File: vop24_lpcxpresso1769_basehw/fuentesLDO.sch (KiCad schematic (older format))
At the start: 21 parts, among them J101 Conn_01x03_Male, U101 MCP1700T-3302E_TT, U102 MCP1700T-3302E_TT, U103 TPS63001

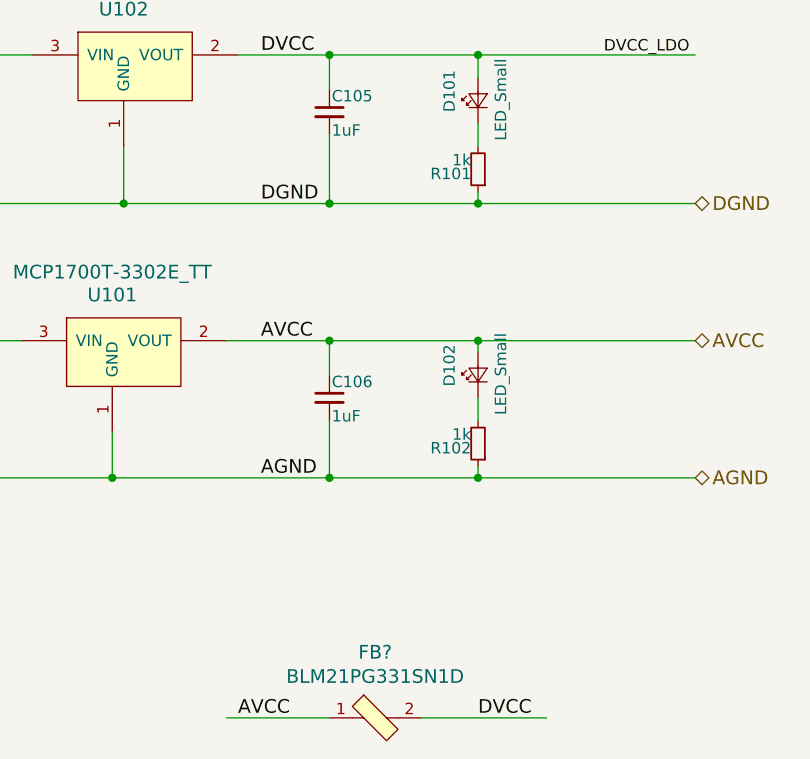
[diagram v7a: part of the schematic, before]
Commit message: Finalizada asociación de todos los footprints. Ver librerías froux-kicad
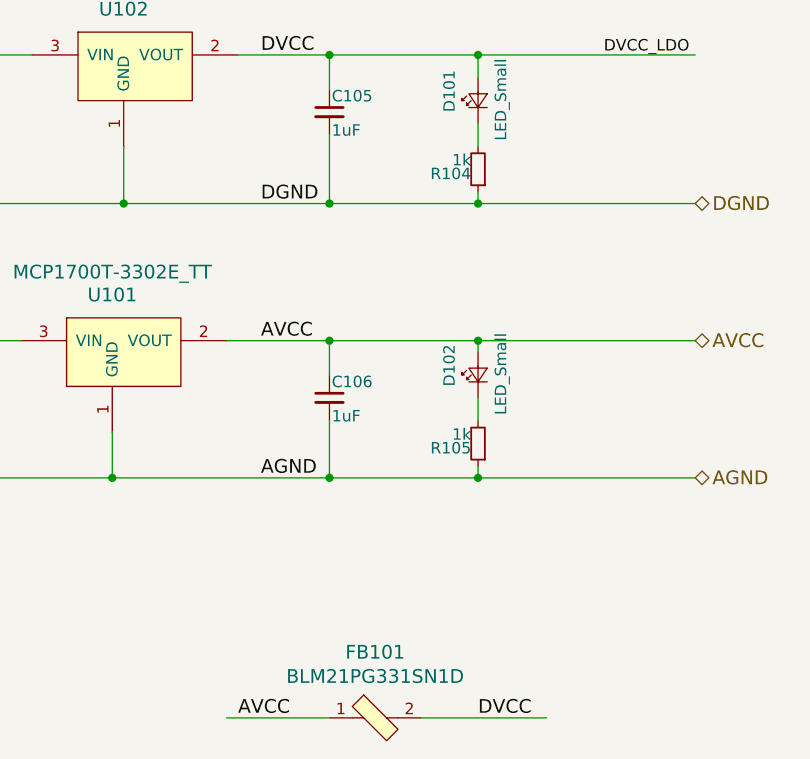
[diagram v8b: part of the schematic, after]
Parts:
- C101, C102, C103, C104, C105, C106, C107, C108: footprint (none) -> Capacitor_SMD:C_0805_2012Metric_Pad1.15x1.40mm_HandSolder
- D101, D102: footprint (none) -> LED_SMD:LED_0805_2012Metric_Pad1.15x1.40mm_HandSolder
- J101: footprint (none) -> Connector_PinHeader_2.54mm:PinHeader_1x03_P2.54mm_Vertical
- R101, R102, R103: footprint (none) -> Resistor_SMD:R_0805_2012Metric_Pad1.15x1.40mm_HandSolder
- R104: renamed from R101; footprint (none) -> Resistor_SMD:R_0805_2012Metric_Pad1.15x1.40mm_HandSolder
- R105: renamed from R102; footprint (none) -> Resistor_SMD:R_0805_2012Metric_Pad1.15x1.40mm_HandSolder
- gave numbers to parts that had none: 1
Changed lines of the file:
@@
 F 0 "C101" H 3510 3820 50  0000 L CNN
 F 1 "1uF" H 3510 3670 50  0000 L CNN
-F 2 "" H 3500 3750 50  0001 C CNN
+F 2 "Capacitor_SMD:C_0805_2012Metric_Pad1.15x1.40mm_HandSolder" H 3500 3750 50  0001 C CNN
 F 3 "" H 3500 3750 50  0001 C CNN
 	1    3500 3750
@@
 F 0 "C105" H 5310 3820 50  0000 L CNN
 F 1 "1uF" H 5310 3670 50  0000 L CNN
-F 2 "" H 5300 3750 50  0001 C CNN
+F 2 "Capacitor_SMD:C_0805_2012Metric_Pad1.15x1.40mm_HandSolder" H 5300 3750 50  0001 C CNN
 F 3 "" H 5300 3750 50  0001 C CNN
 	1    5300 3750
@@
 F 0 "C102" H 3560 5070 50  0000 L CNN
 F 1 "1uF" H 3560 4920 50  0000 L CNN
-F 2 "" H 3550 5000 50  0001 C CNN
+F 2 "Capacitor_SMD:C_0805_2012Metric_Pad1.15x1.40mm_HandSolder" H 3550 5000 50  0001 C CNN
 F 3 "" H 3550 5000 50  0001 C CNN
 	1    3550 5000
@@
 F 0 "C106" H 5310 5070 50  0000 L CNN
 F 1 "1uF" H 5310 4920 50  0000 L CNN
-F 2 "" H 5300 5000 50  0001 C CNN
+F 2 "Capacitor_SMD:C_0805_2012Metric_Pad1.15x1.40mm_HandSolder" H 5300 5000 50  0001 C CNN
 F 3 "" H 5300 5000 50  0001 C CNN
 	1    5300 5000
@@
 F 0 "R101" V 3150 4050 50  0000 L CNN
 F 1 "0" V 3200 4250 50  0000 L CNN
-F 2 "" H 3250 4150 50  0001 C CNN
+F 2 "Resistor_SMD:R_0805_2012Metric_Pad1.15x1.40mm_HandSolder" H 3250 4150 50  0001 C CNN
 F 3 "" H 3250 4150 50  0001 C CNN
 	1    3250 4150
@@
 F 0 "R102" V 3200 5250 50  0000 L CNN
 F 1 "0" V 3250 5500 50  0000 L CNN
-F 2 "" H 3300 5350 50  0001 C CNN
+F 2 "Resistor_SMD:R_0805_2012Metric_Pad1.15x1.40mm_HandSolder" H 3300 5350 50  0001 C CNN
 F 3 "" H 3300 5350 50  0001 C CNN
 	1    3300 5350
@@
 F 0 "D101" H 5900 3825 50  0000 L CNN
 F 1 "LED_Small" H 5775 3600 50  0000 L CNN
-F 2 "" V 5950 3700 50  0001 C CNN
+F 2 "LED_SMD:LED_0805_2012Metric_Pad1.15x1.40mm_HandSolder" V 5950 3700 50  0001 C CNN
 F 3 "" V 5950 3700 50  0001 C CNN
 	1    5950 3700
@@
 $EndComp
 $Comp
-L Device:R_Small R101
+L Device:R_Small R104
 U 1 1 5B38314E
 P 5950 4000
-F 0 "R101" H 5980 4020 50  0000 L CNN
+F 0 "R104" H 5980 4020 50  0000 L CNN
 F 1 "1k" H 5980 3960 50  0000 L CNN
-F 2 "" H 5950 4000 50  0001 C CNN
+F 2 "Resistor_SMD:R_0805_2012Metric_Pad1.15x1.40mm_HandSolder" H 5950 4000 50  0001 C CNN
 F 3 "" H 5950 4000 50  0001 C CNN
 	1    5950 4000
@@
 F 0 "D102" H 5900 5025 50  0000 L CNN
 F 1 "LED_Small" H 5775 4800 50  0000 L CNN
-F 2 "" V 5950 4900 50  0001 C CNN
+F 2 "LED_SMD:LED_0805_2012Metric_Pad1.15x1.40mm_HandSolder" V 5950 4900 50  0001 C CNN
 F 3 "" V 5950 4900 50  0001 C CNN
 	1    5950 4900
@@
 $EndComp
 $Comp
-L Device:R_Small R102
+L Device:R_Small R105
 U 1 1 5B38315C
 P 5950 5200
-F 0 "R102" H 5980 5220 50  0000 L CNN
+F 0 "R105" H 5980 5220 50  0000 L CNN
 F 1 "1k" H 5980 5160 50  0000 L CNN
-F 2 "" H 5950 5200 50  0001 C CNN
+F 2 "Resistor_SMD:R_0805_2012Metric_Pad1.15x1.40mm_HandSolder" H 5950 5200 50  0001 C CNN
 F 3 "" H 5950 5200 50  0001 C CNN
 	1    5950 5200
@@
 F 0 "C107" H 6715 2596 50  0000 L CNN
 F 1 "10uF" H 6715 2505 50  0000 L CNN
-F 2 "" H 6638 2400 50  0001 C CNN
+F 2 "Capacitor_SMD:C_0805_2012Metric_Pad1.15x1.40mm_HandSolder" H 6638 2400 50  0001 C CNN
 F 3 "~" H 6600 2550 50  0001 C CNN
 	1    6600 2550
@@
 F 0 "C104" H 4715 2796 50  0000 L CNN
 F 1 "0.1uF" H 4715 2705 50  0000 L CNN
-F 2 "" H 4638 2600 50  0001 C CNN
+F 2 "Capacitor_SMD:C_0805_2012Metric_Pad1.15x1.40mm_HandSolder" H 4638 2600 50  0001 C CNN
 F 3 "~" H 4600 2750 50  0001 C CNN
 	1    4600 2750
@@
 F 0 "C103" H 3915 2496 50  0000 L CNN
 F 1 "10uF" H 3915 2405 50  0000 L CNN
-F 2 "" H 3838 2300 50  0001 C CNN
+F 2 "Capacitor_SMD:C_0805_2012Metric_Pad1.15x1.40mm_HandSolder" H 3838 2300 50  0001 C CNN
 F 3 "~" H 3800 2450 50  0001 C CNN
 	1    3800 2450
@@
 F 0 "C108" H 7215 2596 50  0000 L CNN
 F 1 "10uF" H 7215 2505 50  0000 L CNN
-F 2 "" H 7138 2400 50  0001 C CNN
+F 2 "Capacitor_SMD:C_0805_2012Metric_Pad1.15x1.40mm_HandSolder" H 7138 2400 50  0001 C CNN
 F 3 "~" H 7100 2550 50  0001 C CNN
 	1    7100 2550
@@
 F 0 "R103" H 4670 2346 50  0000 L CNN
 F 1 "100" H 4670 2255 50  0000 L CNN
-F 2 "" V 4530 2300 50  0001 C CNN
+F 2 "Resistor_SMD:R_0805_2012Metric_Pad1.15x1.40mm_HandSolder" V 4530 2300 50  0001 C CNN
 F 3 "~" H 4600 2300 50  0001 C CNN
 	1    4600 2300
@@
 F 0 "J101" H 9856 3478 50  0000 C CNN
 F 1 "Conn_01x03_Male" H 9856 3387 50  0000 C CNN
-F 2 "" H 9750 3200 50  0001 C CNN
+F 2 "Connector_PinHeader_2.54mm:PinHeader_1x03_P2.54mm_Vertical" H 9750 3200 50  0001 C CNN
 F 3 "~" H 9750 3200 50  0001 C CNN
 	1    9750 3200
@@
 	8900 3200 9550 3200
 $Comp
-L dk_Ferrite-Beads-and-Chips:BLM21PG331SN1D FB?
+L dk_Ferrite-Beads-and-Chips:BLM21PG331SN1D FB101
 U 1 1 5BD41945
 P 5500 6400
-F 0 "FB?" H 5500 6687 60  0000 C CNN
+F 0 "FB101" H 5500 6687 60  0000 C CNN
 F 1 "BLM21PG331SN1D" H 5500 6581 60  0000 C CNN
 F 2 "digikey-footprints:0805" H 5700 6600 60  0001 L CNN
